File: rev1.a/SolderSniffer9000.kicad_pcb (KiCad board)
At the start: 2 copper layers, 31.7 x 80 mm, 25 parts, among them P1 80MM Fan Connector, SW1 SW_POWER, U1 MCP73831, U2 SC4503, X1 USBMICRO

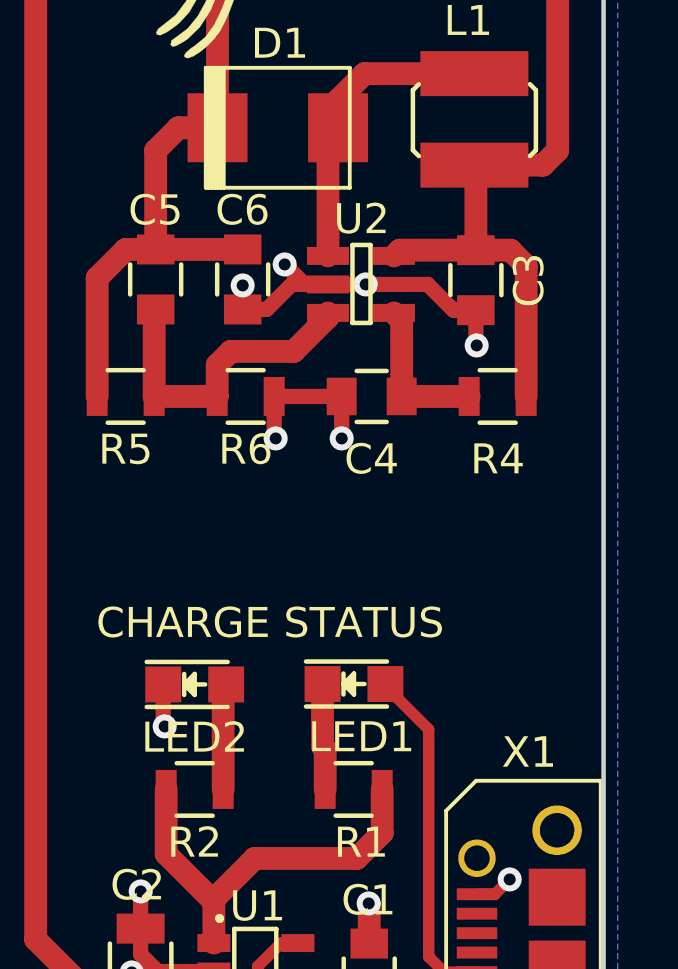
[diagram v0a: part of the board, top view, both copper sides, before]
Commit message: cosmetic changes to silk screen and updated schematic pdf
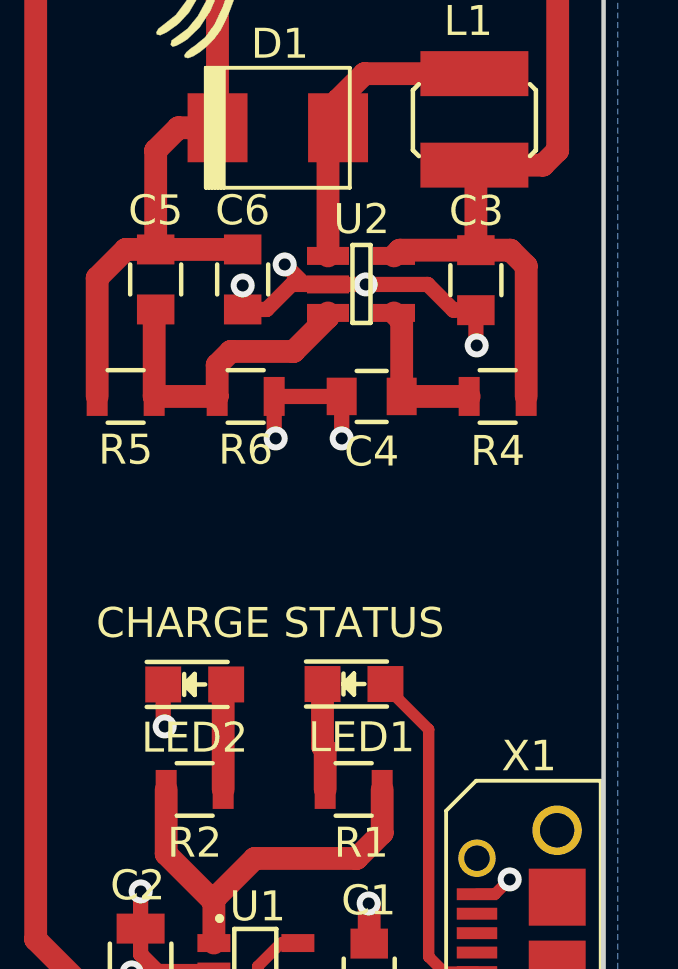
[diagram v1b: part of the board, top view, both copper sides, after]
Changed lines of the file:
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@@
   )
   (setup
-    (last_trace_width 0.381)
+    (last_trace_width 0.25)
     (user_trace_width 0.254)
     (user_trace_width 0.381)
@@
     (pad_to_mask_clearance 0.2)
     (aux_axis_origin 0 0)
-    (visible_elements 7FFEFF5F)
+    (visible_elements 7FFEFF7F)
     (pcbplotparams
       (layerselection 0x010f0_ffffffff)
@@
     (tags "capacitor 0805")
     (attr smd)
-    (fp_text reference C3 (at 0 -1.778 270) (layer F.SilkS)
+    (fp_text reference C3 (at -2.304 -0.016 360) (layer F.SilkS)
       (effects (font (size 1 1) (thickness 0.15)))
     )
@@
     (tags "capacitor 0805")
     (attr smd)
-    (fp_text reference C4 (at 0 -2.1 180) (layer F.SilkS)
+    (fp_text reference C4 (at 0 -1.84 180) (layer F.SilkS)
       (effects (font (size 1 1) (thickness 0.15)))
     )
@@
     (tags "capacitor 0805")
     (attr smd)
-    (fp_text reference C5 (at -2.3 0 360) (layer F.SilkS)
+    (fp_text reference C5 (at -2.3 0) (layer F.SilkS)
       (effects (font (size 1 1) (thickness 0.15)))
     )
@@
     (tags "capacitor 0805")
     (attr smd)
-    (fp_text reference C6 (at -2.3 0 360) (layer F.SilkS)
+    (fp_text reference C6 (at -2.3 0) (layer F.SilkS)
       (effects (font (size 1 1) (thickness 0.15)))
     )
@@
     (tags "resistor 0805")
     (attr smd)
-    (fp_text reference R4 (at 0 -2.1 180) (layer F.SilkS)
+    (fp_text reference R4 (at 0 -1.82 180) (layer F.SilkS)
       (effects (font (size 1 1) (thickness 0.15)))
     )
@@
     (tags "DESCRIPTION: PACKAGE FOR MICRO USB TYPE B CONNECTOR. BASED ON FCI 10118193-0001LF.")
     (attr smd)
-    (fp_text reference X1 (at 6.018 0.472 180) (layer F.SilkS)
+    (fp_text reference X1 (at 5.9 0.47 180) (layer F.SilkS)
       (effects (font (size 1.016 1.016) (thickness 0.1524)))
     )
